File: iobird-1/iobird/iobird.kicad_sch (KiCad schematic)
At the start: 3 parts, among them J1 USB_C_Receptacle_USB2.0, U1 RP2040, U2 W25Q32JVSS

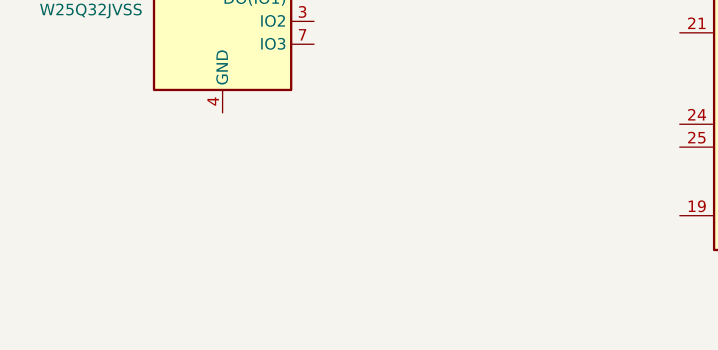
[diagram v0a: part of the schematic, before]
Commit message: add xtal to schematic
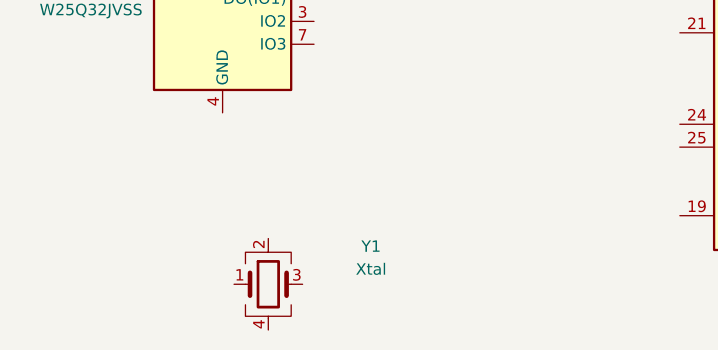
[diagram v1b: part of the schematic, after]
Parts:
- added Y1: Xtal, Crystal:Crystal_SMD_2520-4Pin_2.5x2.0mm, symbol Device:Crystal_GND24
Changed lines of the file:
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@@
+    )
+  )
+  (symbol (lib_id "Device:Crystal_GND24") (at 48.26 120.65 0) (unit 1)
+    (in_bom yes) (on_board yes) (dnp no) (fields_autoplaced)
+    (property "Reference" "Y1" (at 59.69 116.4591 0)
+      (effects (font (size 1.27 1.27)))
+    )
+    (property "Value" "Xtal" (at 59.69 118.9991 0)
+      (effects (font (size 1.27 1.27)))
+    )
+    (property "Footprint" "Crystal:Crystal_SMD_2520-4Pin_2.5x2.0mm" (at 48.26 120.65 0)
+      (effects (font (size 1.27 1.27)) hide)
+    )
+    (property "Datasheet" "https://datasheet.lcsc.com/lcsc/2304140030_Seiko-Epson-Q24FA20H0068700_C90603.pdf" (at 48.26 120.65 0)
+      (effects (font (size 1.27 1.27)) hide)
+    )
+    (pin "1")
+    (pin "2")
+    (pin "4")
+    (pin "3")
+    (instances
+      (project "iobird"
+        (path "/227befc9-6310-476c-924a-cf7b196aa881"
+          (reference "Y1") (unit 1)
+        )
+      )
     )
   )

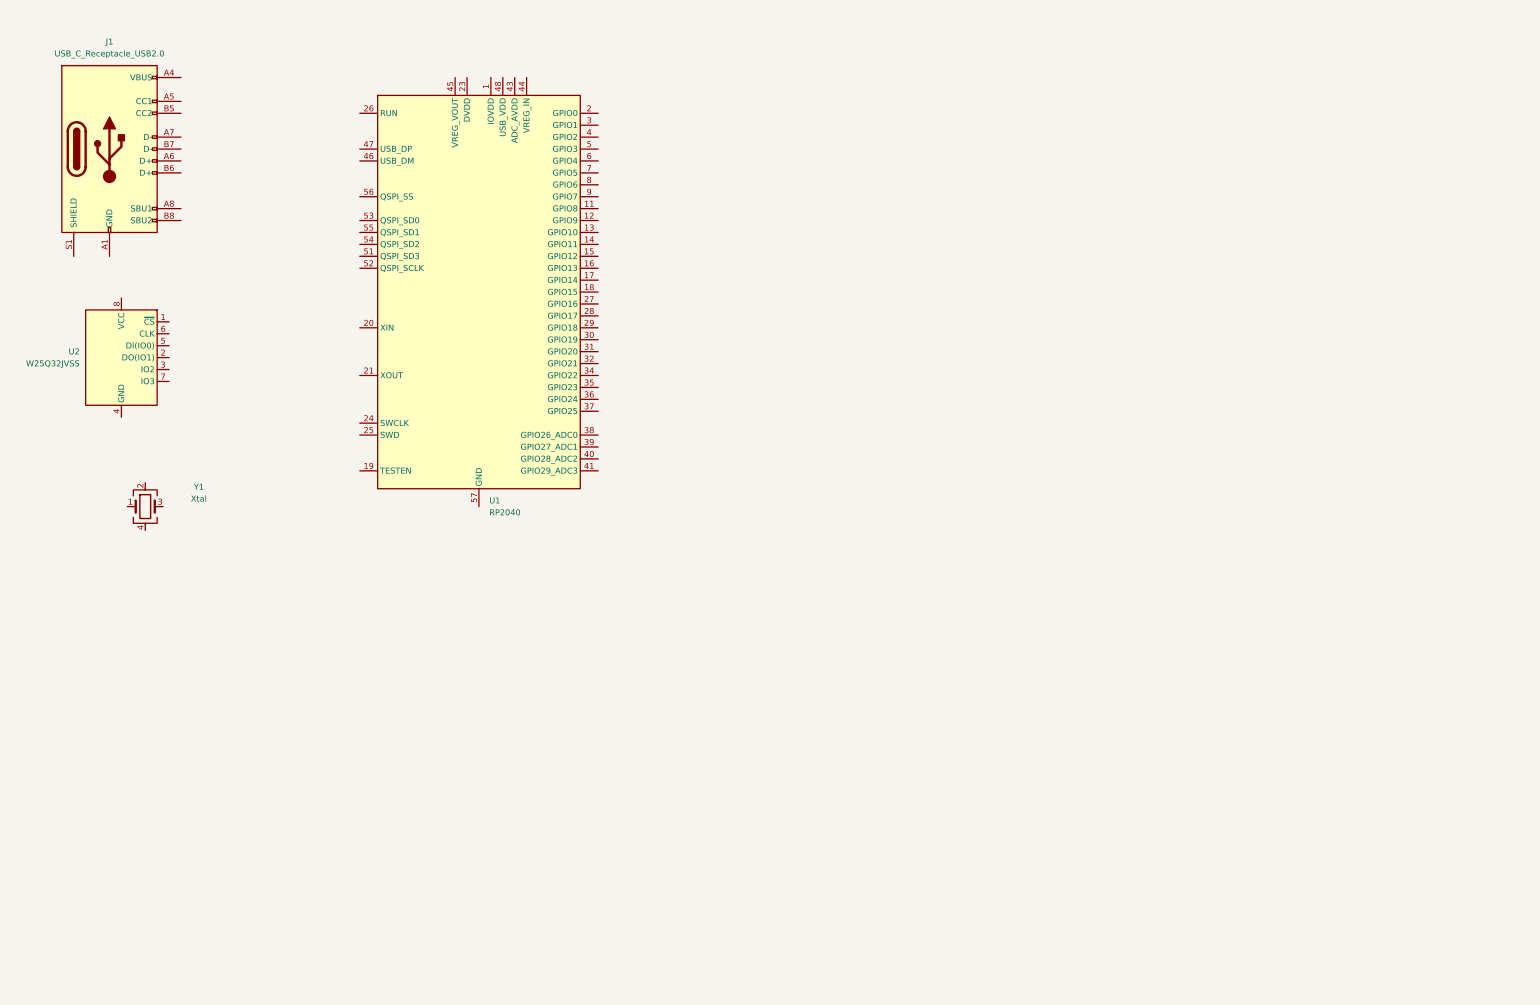
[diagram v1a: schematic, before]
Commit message: filling in more parts
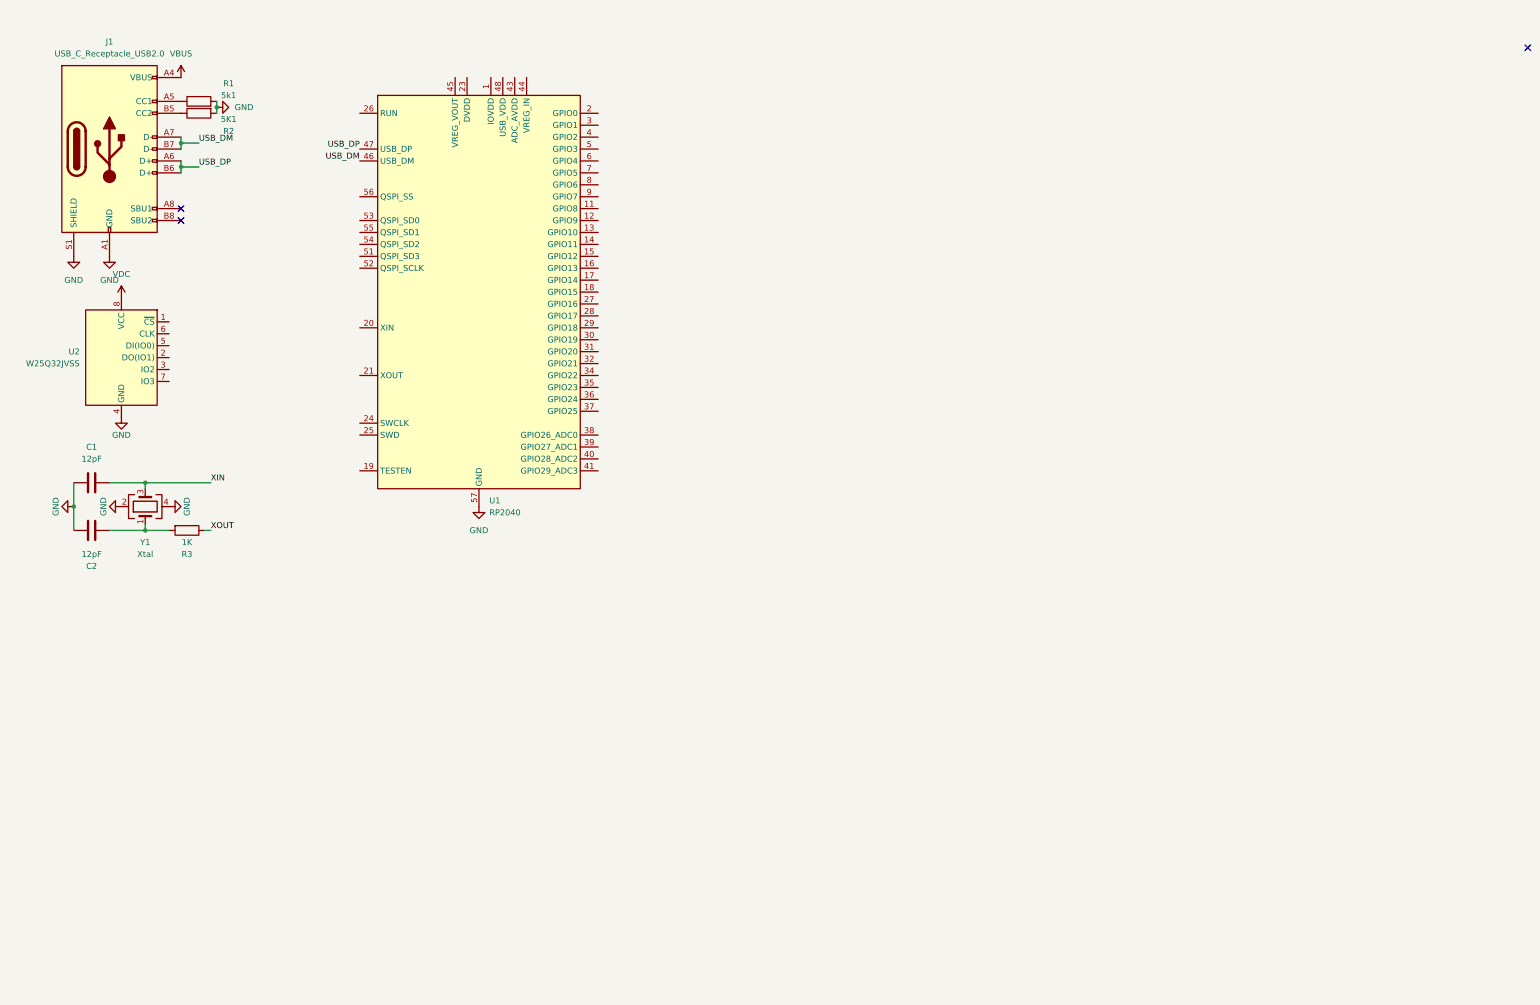
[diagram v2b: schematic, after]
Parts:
- added C1, C2: 12pF, Capacitor_SMD:C_0402_1005Metric, symbol Device:C
- added R1: 5k1, Resistor_SMD:R_0402_1005Metric, symbol Device:R
- added R2: 5K1, Resistor_SMD:R_0402_1005Metric, symbol Device:R
- added R3: 1K, Resistor_SMD:R_0402_1005Metric, symbol Device:R
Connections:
- net GND: now reaches J1.A1 (GND), J1.A12 (GND), J1.B1 (GND), J1.B12 (GND)
- net GND: now also J1.S1 (SHIELD), U1.57 (GND), U2.4 (GND), Y1.2, Y1.4, C1.1, C2.1, R1.2, R2.2
- net VBUS: now reaches J1.A4 (VBUS), J1.A9 (VBUS), J1.B4 (VBUS), J1.B9 (VBUS)
- net at J1.A5 (CC1): now also R1.1
- net USB_DP: now reaches J1.A6 (D+)
- net USB_DP: now also J1.B6 (D+), U1.47 (USB_DP)
- net USB_DM: now reaches J1.A7 (D-)
- net USB_DM: now also J1.B7 (D-), U1.46 (USB_DM)
- net at J1.B5 (CC2): now also R2.1
- net VDC: now reaches U2.8 (VCC)
- net at Y1.1: now also C2.2, R3.2
- net XIN: now reaches Y1.3
- net XIN: now also C1.2
- new net XOUT: R3.1
- no-connect marks 0 -> 3
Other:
- moved on the sheet: Y1

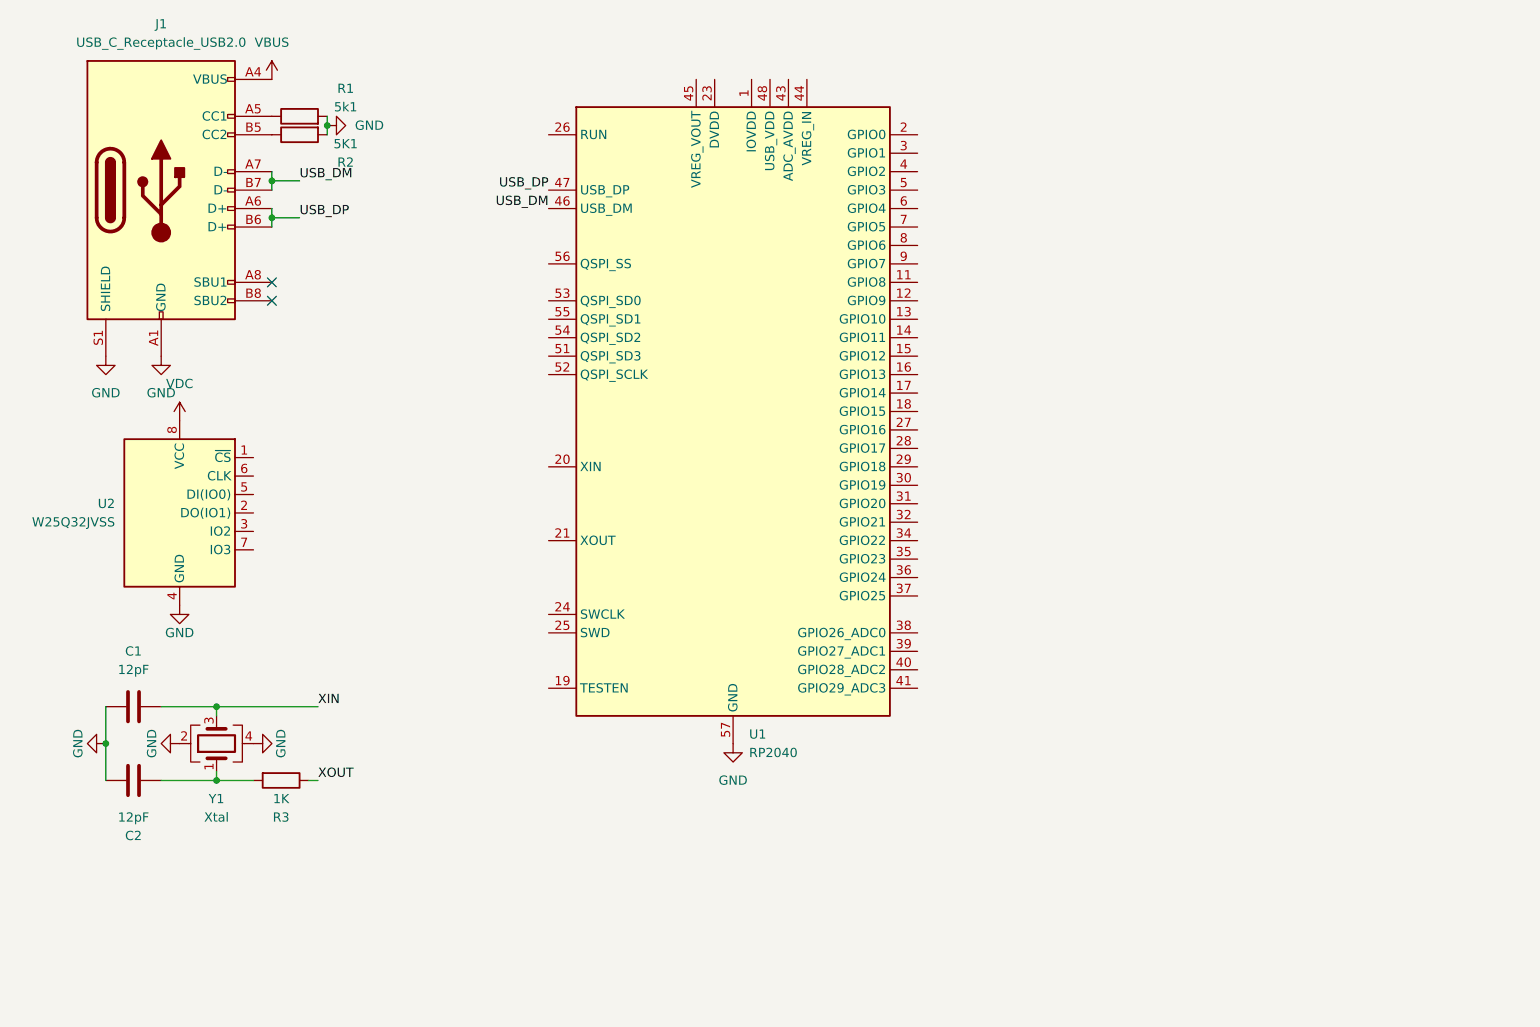
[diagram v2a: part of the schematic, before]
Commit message: more progress
add decoupling capacitors; name them after the pins they are near

add FPC socket and hook up the GPIO pins; the power and ground pins of
the socket match the Raspberry Pi 40 pin HAT header

the 3v3 pin in the middle of the header is notionally the ADC_AVDD
and the GPIO_ADC pins are adjacent

dunno if this will survive board layout
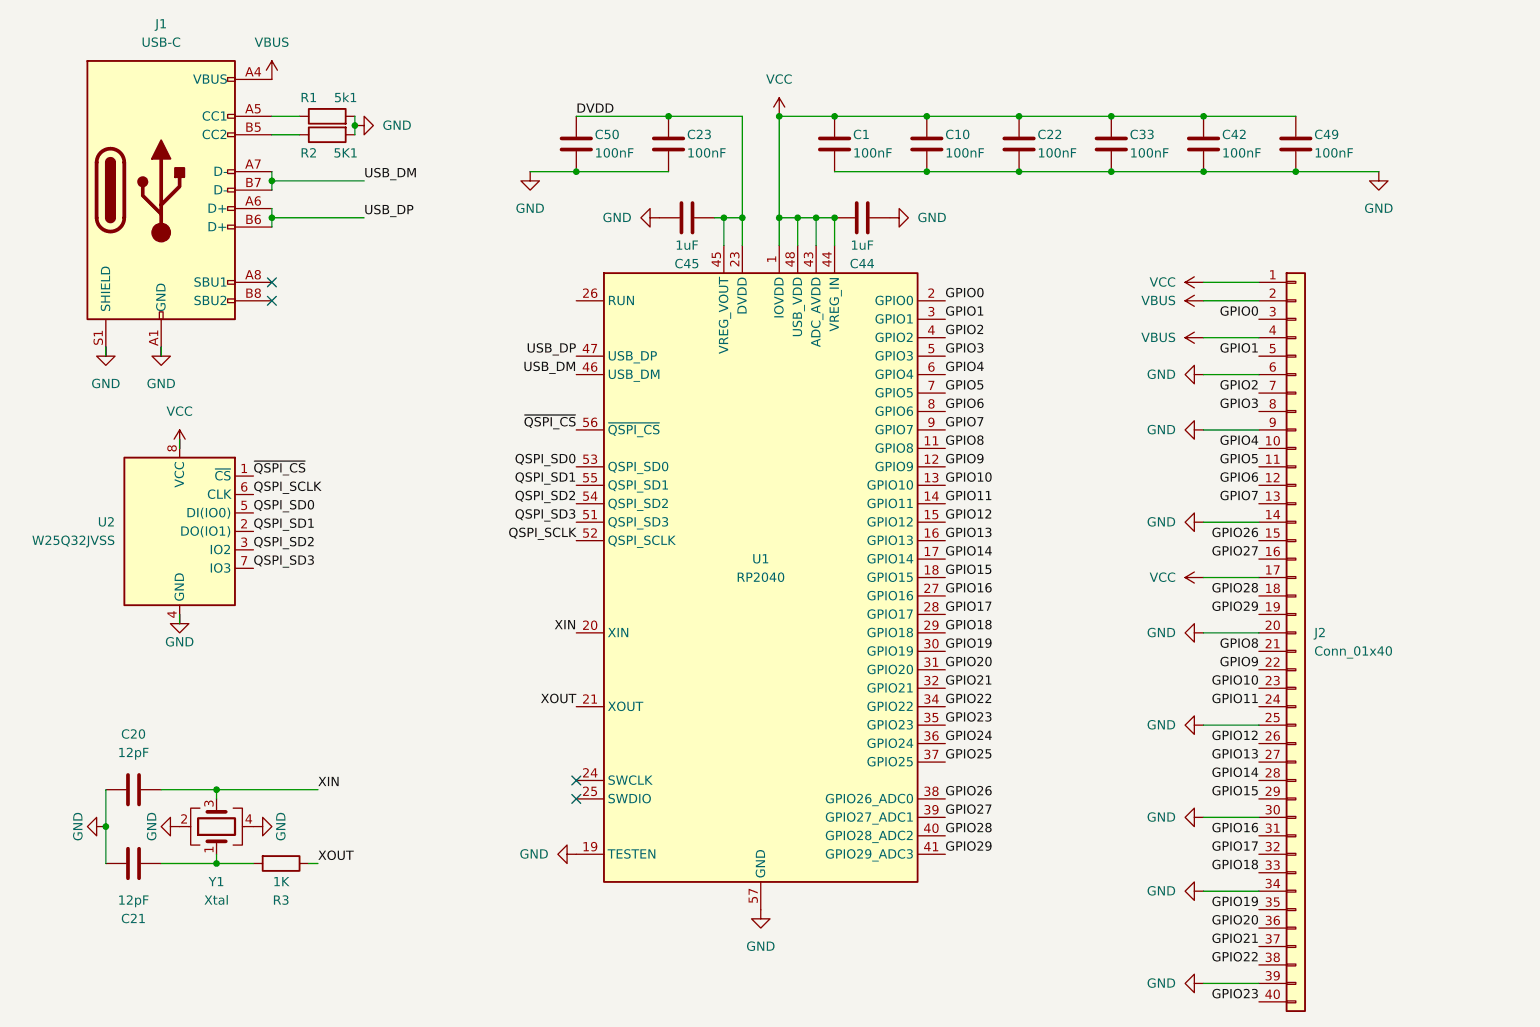
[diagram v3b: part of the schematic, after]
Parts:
- added C1, C10, C22, C23, C33, C42, C49, C50: 100nF, symbol Device:C
- added C44, C45: 1uF, symbol Device:C
- added J2: Conn_01x40, symbol Connector_Generic:Conn_01x40
- J1: value USB_C_Receptacle_USB2.0 -> USB-C
- renumbered C1 to C20, C2 to C21
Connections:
- net VDC is gone; now on net VCC: U2.8 (VCC)
- net GND: now also U1.19 (TESTEN), C1.1, C10.1, C22.1, C23.1, C33.1, C42.1, C44.2, C45.1, C49.1, C50.1, J2.14 (Pin_14), J2.20 (Pin_20), J2.25 (Pin_25), J2.30 (Pin_30), J2.34 (Pin_34), J2.39 (Pin_39), J2.6 (Pin_6), J2.9 (Pin_9)
- net VBUS: now also J2.2 (Pin_2), J2.4 (Pin_4)
- net XIN: now also U1.20 (XIN)
- net XOUT: now also U1.21 (XOUT)
- net VCC: now reaches U1.1 (IOVDD), U1.10 (IOVDD), U1.22 (IOVDD), U1.33 (IOVDD), U1.42 (IOVDD), U1.49 (IOVDD)
- net VCC: now also U1.43 (ADC_AVDD), U1.44 (VREG_IN), U1.48 (USB_VDD), C1.2, C10.2, C22.2, C33.2, C42.2, C44.1, C49.2, J2.1 (Pin_1), J2.17 (Pin_17)
- net GPIO8: now reaches U1.11 (GPIO8)
- net GPIO8: now also J2.21 (Pin_21)
- net GPIO9: now reaches U1.12 (GPIO9)
- net GPIO9: now also J2.22 (Pin_22)
- net GPIO10: now reaches U1.13 (GPIO10)
- net GPIO10: now also J2.23 (Pin_23)
- net GPIO11: now reaches U1.14 (GPIO11)
- net GPIO11: now also J2.24 (Pin_24)
- net GPIO12: now reaches U1.15 (GPIO12)
- net GPIO12: now also J2.26 (Pin_26)
- net GPIO13: now reaches U1.16 (GPIO13)
- net GPIO13: now also J2.27 (Pin_27)
- net GPIO14: now reaches U1.17 (GPIO14)
- net GPIO14: now also J2.28 (Pin_28)
- net GPIO15: now reaches U1.18 (GPIO15)
- net GPIO15: now also J2.29 (Pin_29)
- net GPIO0: now reaches U1.2 (GPIO0)
- net GPIO0: now also J2.3 (Pin_3)
- net DVDD: now reaches U1.23 (DVDD), U1.50 (DVDD)
- net DVDD: now also U1.45 (VREG_VOUT), C23.2, C45.2, C50.2
- net GPIO16: now reaches U1.27 (GPIO16)
- net GPIO16: now also J2.31 (Pin_31)
- net GPIO17: now reaches U1.28 (GPIO17)
- net GPIO17: now also J2.32 (Pin_32)
- net GPIO18: now reaches U1.29 (GPIO18)
- net GPIO18: now also J2.33 (Pin_33)
- net GPIO1: now reaches U1.3 (GPIO1)
- net GPIO1: now also J2.5 (Pin_5)
- net GPIO19: now reaches U1.30 (GPIO19)
- net GPIO19: now also J2.35 (Pin_35)
- net GPIO20: now reaches U1.31 (GPIO20)
- net GPIO20: now also J2.36 (Pin_36)
- net GPIO21: now reaches U1.32 (GPIO21)
- net GPIO21: now also J2.37 (Pin_37)
- net GPIO22: now reaches U1.34 (GPIO22)
- net GPIO22: now also J2.38 (Pin_38)
- net GPIO23: now reaches U1.35 (GPIO23)
- net GPIO23: now also J2.40 (Pin_40)
- net GPIO24: now reaches U1.36 (GPIO24)
- net GPIO25: now reaches U1.37 (GPIO25)
- net GPIO26: now reaches U1.38 (GPIO26_ADC0)
- net GPIO26: now also J2.15 (Pin_15)
- net GPIO27: now reaches U1.39 (GPIO27_ADC1)
- net GPIO27: now also J2.16 (Pin_16)
- net GPIO2: now reaches U1.4 (GPIO2)
- net GPIO2: now also J2.7 (Pin_7)
- net GPIO28: now reaches U1.40 (GPIO28_ADC2)
- net GPIO28: now also J2.18 (Pin_18)
- net GPIO29: now reaches U1.41 (GPIO29_ADC3)
- net GPIO29: now also J2.19 (Pin_19)
- net GPIO3: now reaches U1.5 (GPIO3)
- net GPIO3: now also J2.8 (Pin_8)
- net QSPI_SD3: now reaches U1.51 (QSPI_SD3)
- net QSPI_SD3: now also U2.7 (IO3)
- net QSPI_SCLK: now reaches U1.52 (QSPI_SCLK)
- net QSPI_SCLK: now also U2.6 (CLK)
- net QSPI_SD0: now reaches U1.53 (QSPI_SD0)
- net QSPI_SD0: now also U2.5 (DI(IO0))
- net QSPI_SD2: now reaches U1.54 (QSPI_SD2)
- net QSPI_SD2: now also U2.3 (IO2)
- net QSPI_SD1: now reaches U1.55 (QSPI_SD1)
- net QSPI_SD1: now also U2.2 (DO(IO1))
- net ~{QSPI_CS}: now reaches U1.56 (~{QSPI_CS})
- net ~{QSPI_CS}: now also U2.1 (~{CS})
- net GPIO4: now reaches U1.6 (GPIO4)
- net GPIO4: now also J2.10 (Pin_10)
- net GPIO5: now reaches U1.7 (GPIO5)
- net GPIO5: now also J2.11 (Pin_11)
- net GPIO6: now reaches U1.8 (GPIO6)
- net GPIO6: now also J2.12 (Pin_12)
- net GPIO7: now reaches U1.9 (GPIO7)
- net GPIO7: now also J2.13 (Pin_13)
- no-connect marks 3 -> 5
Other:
- moved on the sheet: C20, C21, R1, R2, R3, U1, U2, Y1
